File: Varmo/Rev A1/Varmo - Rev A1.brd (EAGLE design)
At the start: 160 x 100 mm, 0 parts

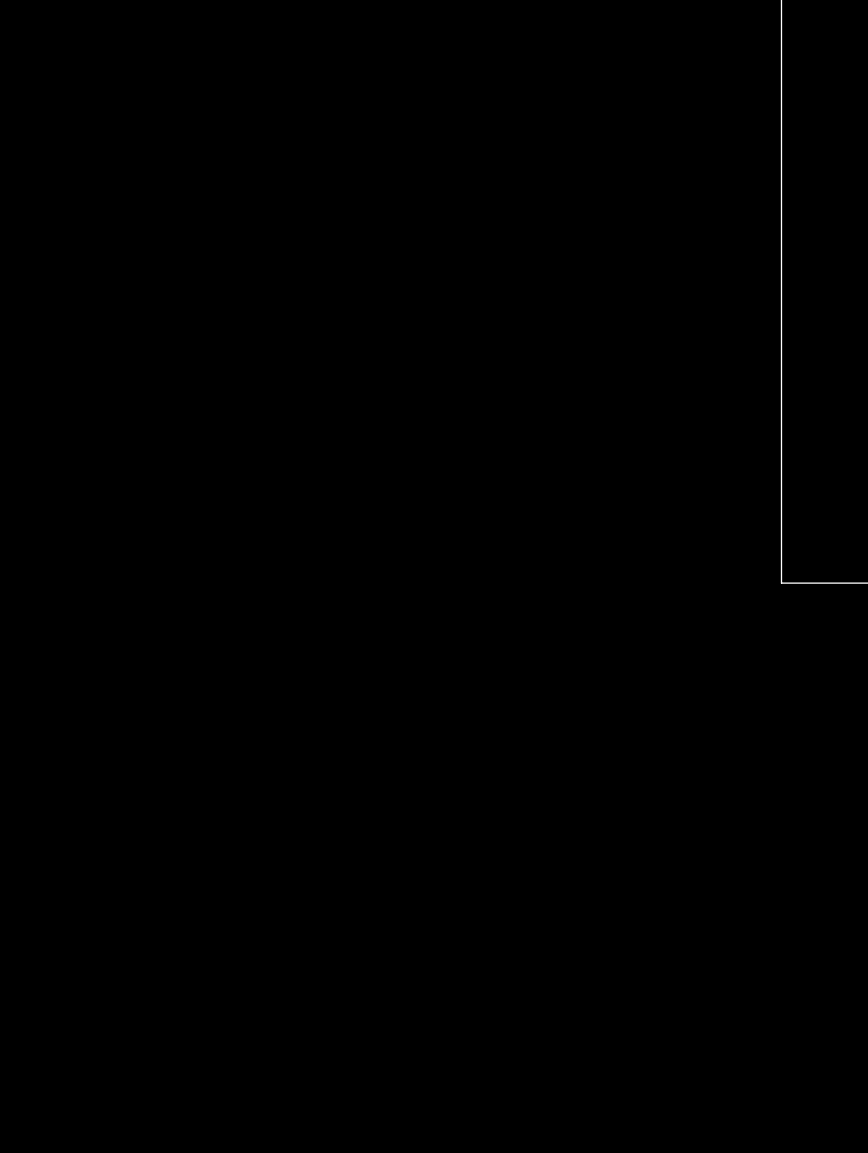
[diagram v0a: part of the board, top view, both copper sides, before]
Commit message: Add NTE0505MC todc-dc-converter library, add 82473C to murata inductor, update Varmo Rev A1 Sch
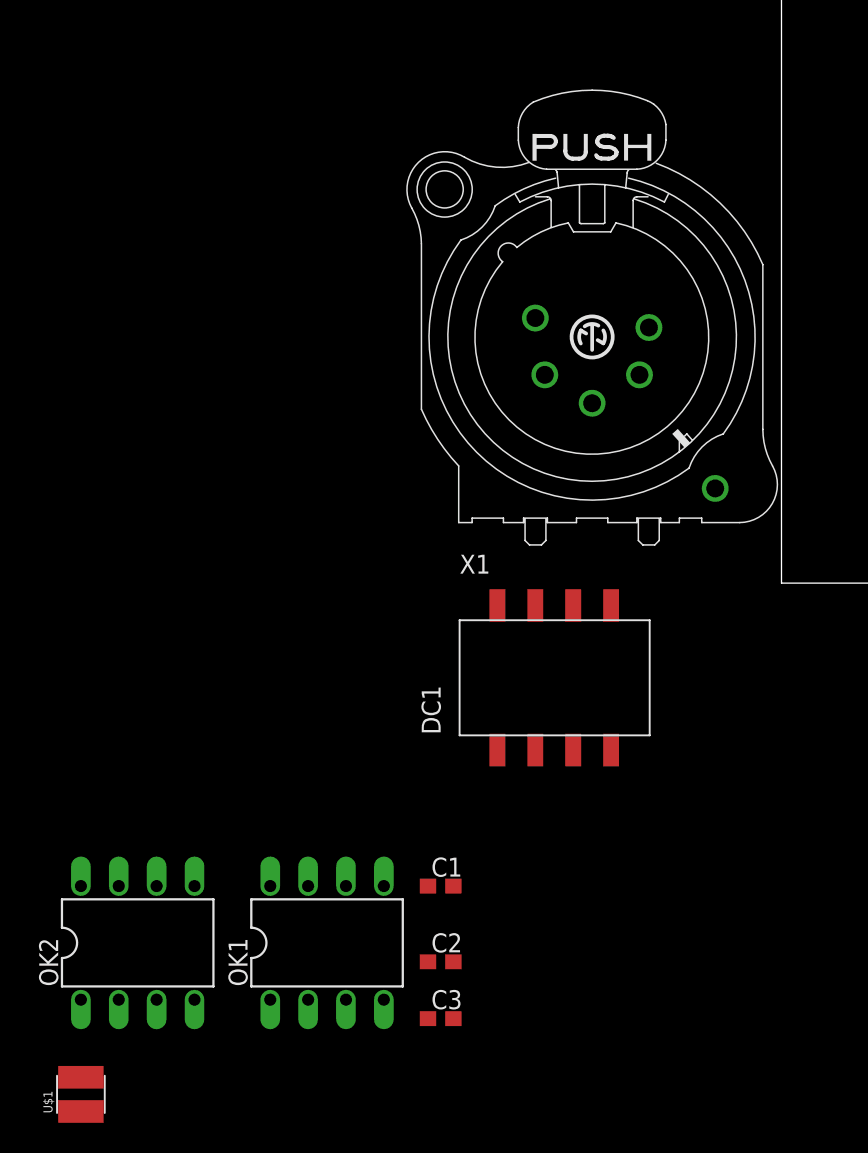
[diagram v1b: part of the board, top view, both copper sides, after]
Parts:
- added C1, C2: 4.7uF, rcl:C0603
- added C3: 0.1uF, rcl:C0603
- added DC1: NTE0505MC, dc-dc-converter:NTE
- added OK1: HCPL2231, optocoupler:DIL08
- added OK2: HCPL2201, optocoupler:DIL08
- added U$1: 47uH, murata-inductance:8200
- added X1: NC5FAV, con-neutrik_ag:NC5FAV
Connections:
- new net +5V: C2.1, C3.1, DC1.3, X1.5
- new net +5V/1: C1.1, OK1.8, U$1.2
- new net ESW3: X1.4
- new net ESW3_RX: OK1.1, X1.2
- new net ESW3_RX_ISO: OK1.7
- new net ESW3_TX: OK1.4, X1.3
- new net ESW3_TX_ISO: OK1.6
- new net GND: C2.2, C3.2, DC1.1, OK1.2, OK1.3, X1.1
- new net GND1: C1.2, DC1.7, OK1.5
- new net GND2: X1.G
- new net N$1: DC1.8, U$1.1

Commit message: Update Varmo schematic Rev A1
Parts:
- removed OK2: HCPL2201, optocoupler:DIL08
- removed X1: NC5FAV, con-neutrik_ag:NC5FAV
- added C4, C5, C6: 0.1uF, rcl:C0603
- added OK3: HCPL2201300E, optocoupler:DIL8-SMD
- added U1: ATMEGA168, atmel:TQFP32-08
- added X2: NC5MAV-SW, con-neutrik_ag:NC5MAV-SW
- added Y1: 10MHz, resonator:RESONATOR-SMD-1:1
- OK1: value HCPL2231 -> HCPL2231300E; device optocoupler:DIL08 -> optocoupler:DIL8-SMD
- moved OK1 59.2 mm to (-78.7, -58.4)
- renumbered U$1 to L1
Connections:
- removed net ESW3: X1.4
- removed net ESW3_RX: OK1.1, X1.2
- new net ESW3_ISO: OK1.4, OK1.6, X2.4
- new net N$2: U1.7, Y1.1
- new net N$3: U1.8, Y1.3
- net +5V: now also OK1.8, X2.5; no longer X1.5
- net +5V/1: now also C4.1, C5.1, C6.1, OK3.8, U1.18, U1.4, U1.6; no longer OK1.8
- net ESW3_RX_ISO: now also OK1.1, X2.2
- net ESW3_TX: now also OK3.2, X2.3; no longer OK1.4, X1.3
- net ESW3_TX_ISO: now also OK3.7; no longer OK1.6
- net GND: now also OK1.5, OK3.3, X2.1; no longer OK1.2, OK1.3, X1.1
- net GND1: now also C4.2, C5.2, C6.2, OK1.2, OK1.3, OK3.5, U1.21, U1.3, U1.5, Y1.2; no longer OK1.5
- net GND2: now also X2.G; no longer X1.G

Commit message: Update Varmo schematic, add library for screw connector , add library for encoder, add library for potentiometre
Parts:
- added C10, C7, C8, C9: 0.1uF, rcl:C0603
- added JP1: F-2X3, con-headers-jp:DIL-100-2X3
- added JP2: (no value), pinhead:1X16
- added R1, R2, R3, R8: 10K, rcl:R0603
- added R10, R7, R9: 4.7k, rcl:R0603
- added R4, R5: 2.2K, rcl:R0603
- added R6: 3313J-1-203E, pot:3313J
- added U$1: EC11E18244AU, encoder:DIP
- added X1: NC5MAH, con-neutrik_ag:NC5MAH
- added X3, X4: SMKDSP_1,5/2, con-phoenix-smkdsp:SMKDSP_1,5/2
- U1: value ATMEGA168 -> ATMEGA328
- X2: value NC5MAV-SW -> SMKDSP_1,5/3; device con-neutrik_ag:NC5MAV-SW -> con-phoenix-smkdsp:SMKDSP_1,5/3
- Y1: value 10MHz -> 8MHz; device resonator:RESONATOR-SMD-1:1 -> resonator:RESONATOR-SMD
- moved OK3 276.2 mm to (154.9, 76.2), turned to 180 degrees
- moved OK1 256.6 mm to (139.7, 76.2)
- moved Y1 224.4 mm to (87.6, 64.8), turned to 180 degrees
- moved L1 188.0 mm to (100.3, 82.5), turned to 270 degrees
- moved C6 183.9 mm to (82.5, 68.6), turned to 90 degrees
- moved C5 182.7 mm to (85.1, 68.6), turned to 90 degrees
- moved C4 181.6 mm to (87.6, 68.6), turned to 90 degrees
- moved C3 180.1 mm to (123.2, 76.2), turned to 270 degrees
- moved C2 174.8 mm to (119.4, 76.2), turned to 270 degrees
- moved U1 170.3 mm to (90.2, 58.4), turned to 270 degrees
- moved C1 154.8 mm to (94.0, 81.3)
- moved X2 154.7 mm to (-91.4, -188.0)
- moved DC1 151.8 mm to (110.5, 78.7), turned to 90 degrees
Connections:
- new net DIRECTION_1: R8.1, X2.1
- new net DIRECTION_2: R7.1, X2.2
- new net ENCODER_A: U1.23
- new net ENCODER_B: U1.24
- new net ENCODER_C: U1.25
- new net MISO: JP1.1, U1.16
- new net MOSI: JP1.3, U1.15
- new net N$4: C9.1, JP1.6
- new net N$5: C10.1, U1.20
- new net PUSH_BUTTON_1: R9.1, X3.1
- new net PUSH_BUTTON_2: R10.1, X4.1
- new net RESET: JP1.4, R1.1, U1.29
- new net SA0: JP2.7, R2.2
- new net SA1: JP2.8, R3.2
- new net SCK: JP1.5, U1.17
- new net SCL: JP2.14, R5.1, U1.28
- new net SDA: JP2.13, R4.1, U1.27
- new net VEE: JP2.15, R6.3
- new net VO: JP2.3, R6.2
- net +5V: now also C8.1, X1.5; no longer X2.5
- net +5V/1: now also C7.1, JP1.2, JP2.2, R1.2, R10.2, R4.2, R5.2, R6.1, R7.2, R8.2, R9.2
- net ESW3_ISO: now also U1.32, X1.4; no longer X2.4
- net ESW3_RX_ISO: now also U1.31, X1.2; no longer X2.2
- net ESW3_TX: now also X1.3; no longer X2.3
- net ESW3_TX_ISO: now also U1.30
- net GND: now also C8.2, X1.1; no longer X2.1
- net GND1: now also C10.2, C7.2, C9.2, JP2.1, JP2.12, JP2.16, R2.1, R3.1, X2.3, X3.2, X4.2
- net GND2: now also X1.G; no longer X2.G
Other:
- board size 160 x 100 mm -> 162.6 x 114.3 mm

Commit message: Update murata inductance.lbr (footprint serie 8400), Update of the Varmo - Rev A1 schematic, Add schmitt trigger x2 and x3 to ti.lbr
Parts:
- added C11, C12, C13, C14, C15, C16: 0.1uF, rcl:C0603
- added LED1, LED2, LED3, LED4: Blue, led:CHIP-LED0603
- added LED5: GRN, led:LED10MM
- added LED6: RED, led:LED10MM
- added R11, R13, R14, R15, R16, R17, R21, R22, R23, R24: 4.7k, rcl:R0603
- added R12: 4.7K, rcl:R0603
- added R18, R19, R20, R25, R26: 0, rcl:R0603
- added U2, U3: SN74LVC2G17DBVR, ti:SOT95P280X145-6N
- added U4, U5: 90814-0210, Molex_By_element14_Batch_1:MOLEX_90814-0210
- R8: value 10K -> 4.7K
- U$1: device encoder:DIP -> encoder:EC11E
- moved U$1 202.2 mm to (-177.8, -353.1)
- moved JP1 43.5 mm to (111.8, 50.8), turned to 270 degrees
- moved U1 5.68 mm to (92.7, 53.3), turned to 315 degrees
- moved R6 2.54 mm to (81.3, 19.1)
- moved X1 2.54 mm to (146.1, 99.1)
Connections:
- removed net ENCODER_C: U1.25
- new net 5V: R24.2, U4.8, X1.5
- new net BUTTON_1: R19.2, U1.23
- new net CONSTRASTE: U1.13
- new net CONTRASTE: R26.2
- new net ENCODER_E: R13.1, U$1.E, U1.2
- new net ESW3: OK1.6, U5.6
- new net ESW3_CMD: R20.1, U1.9
- new net ESW3_RX: OK1.7, U5.2
- new net N$10: C13.1, R16.2, U2.1
- new net N$11: C14.1, R17.2, U2.3
- new net N$12: C12.1, R15.2, U3.3
- new net N$13: C11.1, R14.2, U3.1
- new net N$14: R25.2, R6.2
- new net N$18: LED1.A, R21.1
- new net N$19: LED2.A, R22.1
- new net N$20: LED3.A, R23.1
- new net N$21: LED4.A, R24.1
- new net N$6: R10.1, R15.1, X4.1
- new net N$7: R14.1, R9.1, X3.1
- new net N$8: R16.1, R7.1, X2.1
- new net N$9: R17.1, R8.1, X2.2
- new net RX: R21.2, U4.2, X1.2
- new net TOR: R23.2, U4.6, X1.4
- new net TX: R22.2, U4.4, X1.3
- net +5V: now also U5.8; no longer X1.5
- net +5V/1: now also C15.1, C16.1, R11.2, R12.2, R13.2, U2.5, U3.5
- net DIRECTION_1: now also U1.25, U2.6; no longer R8.1, X2.1
- net DIRECTION_2: now also U1.26, U2.4; no longer R7.1, X2.2
- net ENCODER_A: now also R11.1, U$1.A, U1.32; no longer U1.23
- net ENCODER_B: now also R12.1, U$1.B, U1.1; no longer U1.24
- net ESW3_ISO: now also R18.2, R20.2; no longer OK1.6, U1.32, X1.4
- net ESW3_RX_ISO: no longer OK1.7, X1.2
- net ESW3_TX: now also U5.4; no longer X1.3
- net GND: now also LED1.C, LED2.C, LED3.C, LED4.C, U4.1, U4.10, U4.3, U4.5, U4.7, U4.9, U5.1, U5.10, U5.3, U5.5, U5.7, U5.9
- net GND1: now also C11.2, C12.2, C13.2, C14.2, C15.2, C16.2, U$1.C, U$1.D, U2.2, U3.2
- net PUSH_BUTTON_1: now also R18.1, R19.1, U3.6; no longer R9.1, X3.1
- net PUSH_BUTTON_2: now also U1.24, U3.4; no longer R10.1, X4.1
- net VO: now also R25.1, R26.1; no longer R6.2

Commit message: Update of Varmo - Rev A1 schematic
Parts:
- added R27, R28: 1.5k, rcl:R0603
- R21, R22, R23, R24: value 4.7k -> 1.5k
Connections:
- new net LED_1: R28.2, U1.19
- new net LED_2: R27.2, U1.22
- new net N$15: LED5.A, R27.1
- new net N$16: LED6.A, R28.1
- net GND: now also LED5.K, LED6.K
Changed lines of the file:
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@@
 <element name="LED3" library="led" package="CHIP-LED0603" value="Blue" x="-180.34" y="-320.04"/>
 <element name="LED4" library="led" package="CHIP-LED0603" value="Blue" x="-185.42" y="-320.04"/>
-<element name="R21" library="rcl" package="R0603" value="4.7k" x="-185.42" y="-325.12"/>
-<element name="R22" library="rcl" package="R0603" value="4.7k" x="-185.42" y="-330.2"/>
-<element name="R23" library="rcl" package="R0603" value="4.7k" x="-185.42" y="-335.28"/>
-<element name="R24" library="rcl" package="R0603" value="4.7k" x="-185.42" y="-340.36"/>
+<element name="R21" library="rcl" package="R0603" value="1.5k" x="-185.42" y="-325.12"/>
+<element name="R22" library="rcl" package="R0603" value="1.5k" x="-185.42" y="-330.2"/>
+<element name="R23" library="rcl" package="R0603" value="1.5k" x="-185.42" y="-335.28"/>
+<element name="R24" library="rcl" package="R0603" value="1.5k" x="-185.42" y="-340.36"/>
 <element name="U$1" library="encoder" package="EC11E" value="EC11E18244AU" x="-177.8" y="-353.06">
 <attribute name="MPN" value="EC11E18244AU" x="-177.8" y="-353.06" size="1.778" layer="27" display="off"/>
@@
 <element name="LED5" library="led" package="LED10MM" value="GRN" x="-180.34" y="-381"/>
 <element name="LED6" library="led" package="LED10MM" value="RED" x="-180.34" y="-393.7"/>
+<element name="R27" library="rcl" package="R0603" value="1.5k" x="-185.42" y="-403.86"/>
+<element name="R28" library="rcl" package="R0603" value="1.5k" x="-185.42" y="-408.94"/>
 </elements>
 <signals>
@@
 <contactref element="LED2" pad="C"/>
 <contactref element="LED3" pad="C"/>
+<contactref element="LED5" pad="K"/>
+<contactref element="LED6" pad="K"/>
 <wire x1="-180.34" y1="-319.29" x2="-185.42" y2="-319.29" width="0" layer="19" extent="1-1"/>
 <wire x1="-175.26" y1="-319.29" x2="-180.34" y2="-319.29" width="0" layer="19" extent="1-1"/>
@@
 <wire x1="-134.62" y1="-314.96" x2="-137.16" y2="-314.96" width="0" layer="19" extent="1-1"/>
 <wire x1="-133.35" y1="-308.9656" x2="-134.62" y2="-314.96" width="0" layer="19" extent="1-1"/>
+<wire x1="-179.07" y1="-381" x2="-180.34" y2="-319.29" width="0" layer="19" extent="1-1"/>
+<wire x1="-179.07" y1="-393.7" x2="-179.07" y2="-381" width="0" layer="19" extent="1-1"/>
 <wire x1="115.34" y1="74.93" x2="-133.35" y2="-308.9656" width="0" layer="19" extent="1-1"/>
 <wire x1="119.38" y1="75.35" x2="115.34" y2="74.93" width="0" layer="19" extent="1-1"/>
@@
 <contactref element="U1" pad="13"/>
 </signal>
+<signal name="N$15">
+<contactref element="LED5" pad="A"/>
+<contactref element="R27" pad="1"/>
+<wire x1="-181.61" y1="-381" x2="-186.27" y2="-403.86" width="0" layer="19" extent="1-1"/>
+</signal>
+<signal name="N$16">
+<contactref element="LED6" pad="A"/>
+<contactref element="R28" pad="1"/>
+<wire x1="-181.61" y1="-393.7" x2="-186.27" y2="-408.94" width="0" layer="19" extent="1-1"/>
+</signal>
+<signal name="LED_1">
+<contactref element="U1" pad="19"/>
+<contactref element="R28" pad="2"/>
+<wire x1="-184.57" y1="-408.94" x2="94.896796875" y2="49.45614375" width="0" layer="19" extent="1-1"/>
+</signal>
+<signal name="LED_2">
+<contactref element="R27" pad="2"/>
+<contactref element="U1" pad="22"/>
+<wire x1="-184.57" y1="-403.86" x2="96.593853125" y2="51.1532" width="0" layer="19" extent="1-1"/>
+</signal>
 </signals>
